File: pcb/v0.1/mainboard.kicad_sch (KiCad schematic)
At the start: 15 parts, among them J1 Conn_01x02_Pin, J2 TYPE_C_Receptacle, J3 Conn_01x04_Pin, U1 AP2112K-3.3TRG1

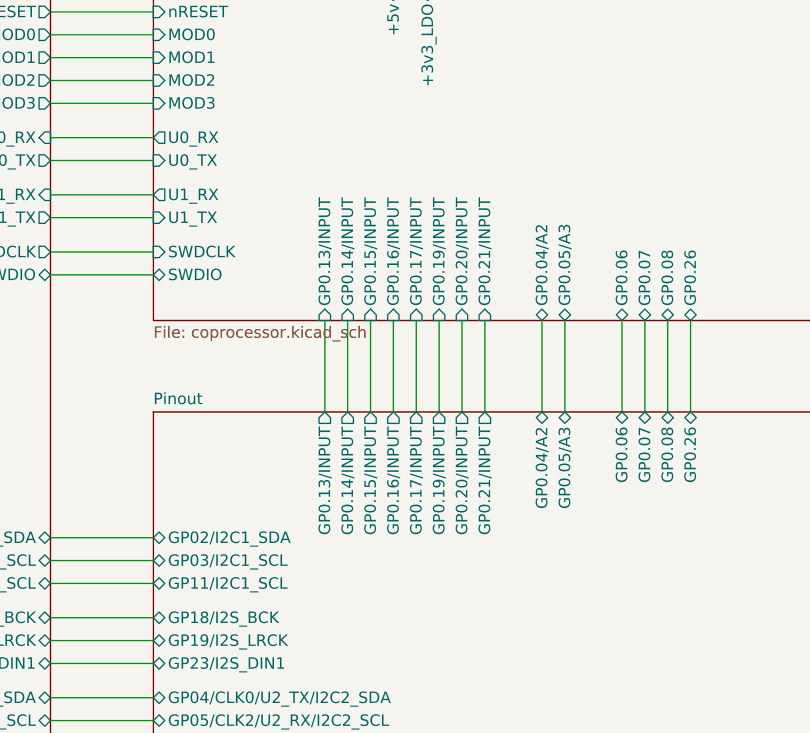
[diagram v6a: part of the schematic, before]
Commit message: Remove input only limitation on NRF pins (logic analyser)
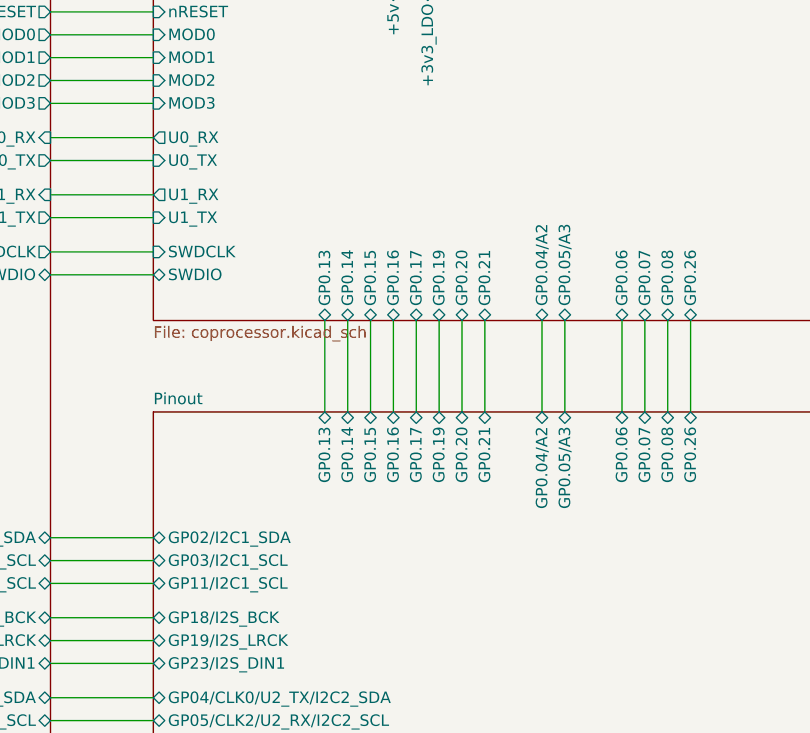
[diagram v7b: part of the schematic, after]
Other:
- sheet Co processor ports: added GP0.13, GP0.14, GP0.15, GP0.16, GP0.17, GP0.19, GP0.20, GP0.21; removed GP0.13/INPUT, GP0.14/INPUT, GP0.15/INPUT, GP0.16/INPUT, GP0.17/INPUT, GP0.19/INPUT, GP0.20/INPUT, GP0.21/INPUT
- sheet Pinout ports: added GP0.13, GP0.14, GP0.15, GP0.16, GP0.17, GP0.19, GP0.20, GP0.21; removed GP0.13/INPUT, GP0.14/INPUT, GP0.15/INPUT, GP0.16/INPUT, GP0.17/INPUT, GP0.19/INPUT, GP0.20/INPUT, GP0.21/INPUT
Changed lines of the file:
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@@
-			)
-		)
-		(pin "GP0.13{slash}INPUT" input
-			(at 213.36 64.77 270)
-			(effects
-				(font
-					(size 1.27 1.27)
-				)
-				(justify left)
-			)
-		)
-		(pin "GP0.14{slash}INPUT" input
-			(at 215.9 64.77 270)
-			(effects
-				(font
-					(size 1.27 1.27)
-				)
-				(justify left)
-			)
-		)
-		(pin "GP0.15{slash}INPUT" input
-			(at 218.44 64.77 270)
-			(effects
-				(font
-					(size 1.27 1.27)
-				)
-				(justify left)
 			)
 		)
@@
 			)
 		)
-		(pin "GP0.17{slash}INPUT" input
-			(at 223.52 64.77 270)
-			(effects
-				(font
-					(size 1.27 1.27)
-				)
-				(justify left)
-			)
-		)
-		(pin "GP0.19{slash}INPUT" input
-			(at 226.06 64.77 270)
-			(effects
-				(font
-					(size 1.27 1.27)
-				)
-				(justify left)
-			)
-		)
 		(pin "GP0.06" bidirectional
 			(at 246.38 64.77 270)
@@
 			)
 		)
-		(pin "GP0.20{slash}INPUT" input
-			(at 228.6 64.77 270)
-			(effects
-				(font
-					(size 1.27 1.27)
-				)
-				(justify left)
-			)
-		)
-		(pin "GP0.16{slash}INPUT" input
-			(at 220.98 64.77 270)
-			(effects
-				(font
-					(size 1.27 1.27)
-				)
-				(justify left)
-			)
-		)
-		(pin "GP0.21{slash}INPUT" input
-			(at 231.14 64.77 270)
-			(effects
-				(font
-					(size 1.27 1.27)
-				)
-				(justify left)
-			)
-		)
 		(pin "GP0.08" bidirectional
 			(at 251.46 64.77 270)
@@
 		(pin "GP0.05{slash}A3" bidirectional
 			(at 240.03 64.77 270)
+			(effects
+				(font
+					(size 1.27 1.27)
+				)
+				(justify left)
+			)
+		)
+		(pin "GP0.16" bidirectional
+			(at 220.98 64.77 270)
+			(effects
+				(font
+					(size 1.27 1.27)
+				)
+				(justify left)
+			)
+		)
+		(pin "GP0.21" bidirectional
+			(at 231.14 64.77 270)
+			(effects
+				(font
+					(size 1.27 1.27)
+				)
+				(justify left)
+			)
+		)
+		(pin "GP0.20" bidirectional
+			(at 228.6 64.77 270)
+			(effects
+				(font
+					(size 1.27 1.27)
+				)
+				(justify left)
+			)
+		)
+		(pin "GP0.19" bidirectional
+			(at 226.06 64.77 270)
+			(effects
+				(font
+					(size 1.27 1.27)
+				)
+				(justify left)
+			)
+		)
+		(pin "GP0.17" bidirectional
+			(at 223.52 64.77 270)
+			(effects
+				(font
+					(size 1.27 1.27)
+				)
+				(justify left)
+			)
+		)
+		(pin "GP0.14" bidirectional
+			(at 215.9 64.77 270)
+			(effects
+				(font
+					(size 1.27 1.27)
+				)
+				(justify left)
+			)
+		)
+		(pin "GP0.13" bidirectional
+			(at 213.36 64.77 270)
+			(effects
+				(font
+					(size 1.27 1.27)
+				)
+				(justify left)
+			)
+		)
+		(pin "GP0.15" bidirectional
+			(at 218.44 64.77 270)
 			(effects
 				(font
@@
 			)
 		)
-		(pin "GP0.16{slash}INPUT" output
-			(at 220.98 74.93 90)
-			(effects
-				(font
-					(size 1.27 1.27)
-				)
-				(justify right)
-			)
-		)
 		(pin "GP0.04{slash}A2" bidirectional
 			(at 237.49 74.93 90)
@@
 			)
 		)
-		(pin "GP0.19{slash}INPUT" output
-			(at 226.06 74.93 90)
-			(effects
-				(font
-					(size 1.27 1.27)
-				)
-				(justify right)
-			)
-		)
 		(pin "GP9" bidirectional
 			(at 194.31 113.03 180)
@@
 			)
 		)
-		(pin "GP0.20{slash}INPUT" output
-			(at 228.6 74.93 90)
-			(effects
-				(font
-					(size 1.27 1.27)
-				)
-				(justify right)
-			)
-		)
 		(pin "GP0.07" bidirectional
 			(at 248.92 74.93 90)
@@
 			)
 		)
-		(pin "GP0.13{slash}INPUT" output
-			(at 213.36 74.93 90)
-			(effects
-				(font
-					(size 1.27 1.27)
-				)
-				(justify right)
-			)
-		)
-		(pin "GP0.17{slash}INPUT" output
-			(at 223.52 74.93 90)
-			(effects
-				(font
-					(size 1.27 1.27)
-				)
-				(justify right)
-			)
-		)
 		(pin "+3v3_LDO" input
 			(at 270.51 115.57 0)
@@
 			)
 		)
-		(pin "GP0.21{slash}INPUT" output
-			(at 231.14 74.93 90)
-			(effects
-				(font
-					(size 1.27 1.27)
-				)
-				(justify right)
-			)
-		)
 		(pin "GP17" bidirectional
 			(at 194.31 115.57 180)
@@
 			)
 		)
-		(pin "GP0.15{slash}INPUT" output
-			(at 218.44 74.93 90)
-			(effects
-				(font
-					(size 1.27 1.27)
-				)
-				(justify right)
-			)
-		)
 		(pin "GP23{slash}I2S_DIN1" bidirectional
 			(at 194.31 102.87 180)
@@
 			)
 		)
-		(pin "GP0.14{slash}INPUT" output
-			(at 215.9 74.93 90)
-			(effects
-				(font
-					(size 1.27 1.27)
-				)
-				(justify right)
-			)
-		)
 		(pin "GP0.06" bidirectional
 			(at 246.38 74.93 90)
 			(effects
 				(font
+					(size 1.27 1.27)
+				)
+				(justify right)
+			)
+		)
+		(pin "GP0.15" bidirectional
+			(at 218.44 74.93 90)
+			(effects
+				(font
+					(size 1.27 1.27)
+				)
+				(justify right)
+			)
+		)
+		(pin "GP0.19" bidirectional
+			(at 226.06 74.93 90)
+			(effects
+				(font
+					(size 1.27 1.27)
+				)
+				(justify right)
+			)
+		)
+		(pin "GP0.21" bidirectional
+			(at 231.14 74.93 90)
+			(effects
+				(font
+					(size 1.27 1.27)
+				)
+				(justify right)
+			)
+		)
+		(pin "GP0.20" bidirectional
+			(at 228.6 74.93 90)
+			(effects
+				(font
+					(size 1.27 1.27)
+				)
+				(justify right)
+			)
+		)
+		(pin "GP0.14" bidirectional
+			(at 215.9 74.93 90)
+			(effects
+				(font
+					(size 1.27 1.27)
+				)
+				(justify right)
+			)
+		)
+		(pin "GP0.16" bidirectional
+			(at 220.98 74.93 90)
+			(effects
+				(font
+					(size 1.27 1.27)
+				)
+				(justify right)
+			)
+		)
+		(pin "GP0.13" bidirectional
+			(at 213.36 74.93 90)
+			(effects
+				(font
+					(size 1.27 1.27)
+				)
+				(justify right)
+			)
+		)
+		(pin "GP0.17" bidirectional
+			(at 223.52 74.93 90)
+			(effects
+				(font
